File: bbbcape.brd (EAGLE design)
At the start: 54.6 x 71.8 mm, 11 parts

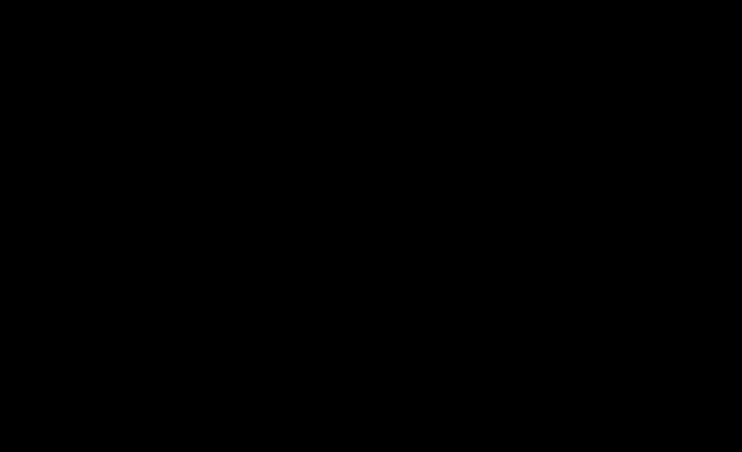
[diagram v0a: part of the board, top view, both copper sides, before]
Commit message: Connected motors.
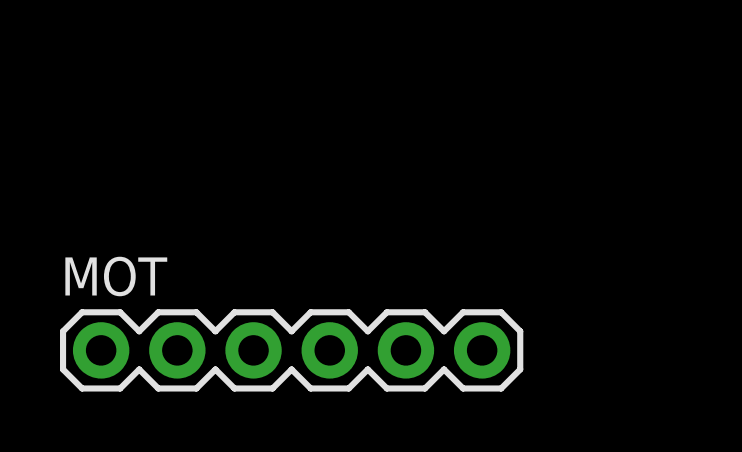
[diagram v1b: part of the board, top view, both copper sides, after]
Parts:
- added MOT: (no value), SparkFun-Connectors:1X06
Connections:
- net BC renamed BCOM
- removed net B0: BPR.2
- removed net B1: BPR.3
- removed net B2: BPR.4
- removed net B3: BPR.5
- new net BAR_DR: BBB.9, BPR.4
- new net BAR_GA: BBB.10, BPR.5
- new net BAV_DR: BBB.7, BPR.2
- new net BAV_GA: BBB.8, BPR.3
- new net DIR_MOT_DR0: BBB.58, MOT.1
- new net DIR_MOT_DR1: BBB.59, MOT.2
- new net DIR_MOT_GA0: BBB.61, MOT.4
- new net DIR_MOT_GA1: BBB.67, MOT.5
- new net PWM_MOT_DR: BBB.60, MOT.3
- new net PWM_MOT_GA: BBB.62, MOT.6
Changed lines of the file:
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@@
 <attribute name="PROD_ID" value="CONN-08437" x="-33.02" y="90.17" size="1.778" layer="27" display="off"/>
+</element>
+<element name="MOT" library="SparkFun-Connectors" package="1X06" value="" x="-82.55" y="-29.21">
+<attribute name="PROD_ID" value="CONN-08437" x="-82.55" y="-29.21" size="1.778" layer="27" display="off"/>
 </element>
 </elements>
@@
 <contactref element="SHLD1" pad="7"/>
 </signal>
-<signal name="BC">
+<signal name="BCOM">
 <contactref element="BPR" pad="1"/>
 <contactref element="R1" pad="P$1"/>
 <wire x1="-66.04" y1="95.25" x2="-41.91" y2="95.25" width="0" layer="19" extent="1-1"/>
 </signal>
-<signal name="B0">
+<signal name="BAV_DR">
 <contactref element="BPR" pad="2"/>
+<contactref element="BBB" pad="7"/>
+<wire x1="3.81" y1="8.89" x2="-39.37" y2="95.25" width="0" layer="19" extent="1-1"/>
 </signal>
-<signal name="B1">
+<signal name="BAV_GA">
 <contactref element="BPR" pad="3"/>
+<contactref element="BBB" pad="8"/>
+<wire x1="1.27" y1="8.89" x2="-36.83" y2="95.25" width="0" layer="19" extent="1-1"/>
 </signal>
-<signal name="B2">
+<signal name="BAR_DR">
 <contactref element="BPR" pad="4"/>
+<contactref element="BBB" pad="9"/>
+<wire x1="3.81" y1="11.43" x2="-34.29" y2="95.25" width="0" layer="19" extent="1-1"/>
 </signal>
-<signal name="B3">
+<signal name="BAR_GA">
 <contactref element="BPR" pad="5"/>
+<contactref element="BBB" pad="10"/>
+<wire x1="1.27" y1="11.43" x2="-31.75" y2="95.25" width="0" layer="19" extent="1-1"/>
 </signal>
 <signal name="3.3V">
@@
 <wire x1="49.53" y1="3.81" x2="52.07" y2="3.81" width="0" layer="19" extent="1-1"/>
 </signal>
+<signal name="DIR_MOT_DR0">
+<contactref element="BBB" pad="58"/>
+<contactref element="MOT" pad="1"/>
+<wire x1="49.53" y1="13.97" x2="-82.55" y2="-29.21" width="0" layer="19" extent="1-1"/>
+</signal>
+<signal name="PWM_MOT_DR">
+<contactref element="BBB" pad="60"/>
+<contactref element="MOT" pad="3"/>
+<wire x1="49.53" y1="16.51" x2="-77.47" y2="-29.21" width="0" layer="19" extent="1-1"/>
+</signal>
+<signal name="PWM_MOT_GA">
+<contactref element="BBB" pad="62"/>
+<contactref element="MOT" pad="6"/>
+<wire x1="49.53" y1="19.05" x2="-69.85" y2="-29.21" width="0" layer="19" extent="1-1"/>
+</signal>
+<signal name="DIR_MOT_DR1">
+<contactref element="BBB" pad="59"/>
+<contactref element="MOT" pad="2"/>
+<wire x1="52.07" y1="16.51" x2="-80.01" y2="-29.21" width="0" layer="19" extent="1-1"/>
+</signal>
+<signal name="DIR_MOT_GA0">
+<contactref element="BBB" pad="61"/>
+<contactref element="MOT" pad="4"/>
+<wire x1="52.07" y1="19.05" x2="-74.93" y2="-29.21" width="0" layer="19" extent="1-1"/>
+</signal>
+<signal name="DIR_MOT_GA1">
+<contactref element="BBB" pad="67"/>
+<contactref element="MOT" pad="5"/>
+<wire x1="52.07" y1="26.67" x2="-72.39" y2="-29.21" width="0" layer="19" extent="1-1"/>
+</signal>
 </signals>

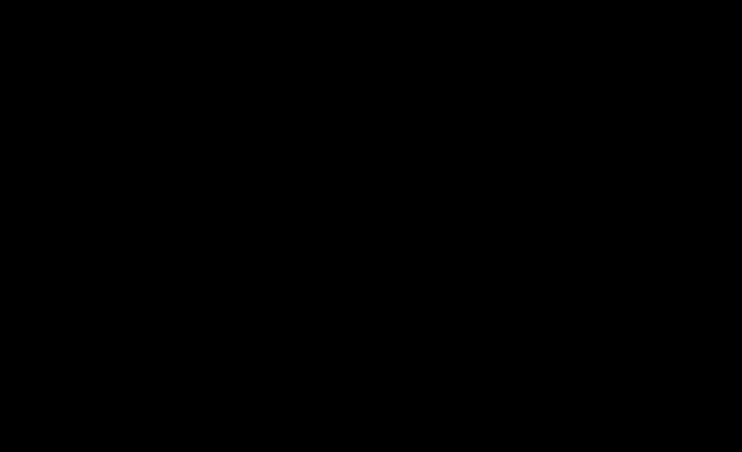
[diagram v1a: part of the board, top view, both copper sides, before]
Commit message: Connected CMUCam2+.
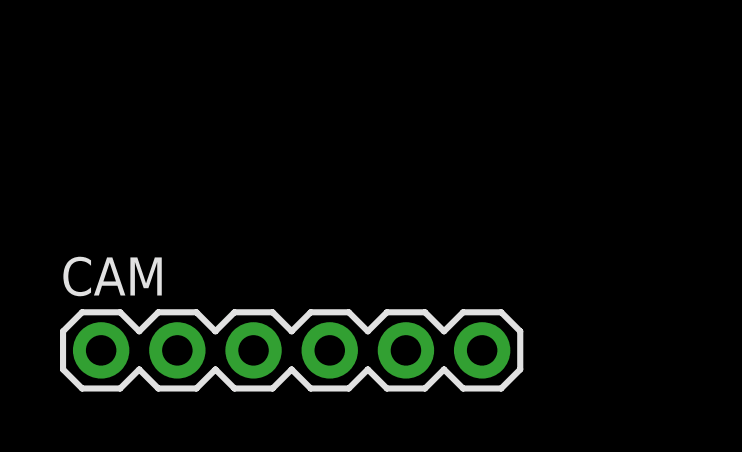
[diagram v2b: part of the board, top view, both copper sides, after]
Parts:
- added CAM: (no value), SparkFun-Connectors:1X06
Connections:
- new net UART1_RX: BBB.72, CAM.6
- new net UART1_TX: BBB.70, CAM.5
- new net VCC: CAM.2
- net 3.3V: now also CAM.3
- net 5V: now also CAM.4
- net GND: now also CAM.1
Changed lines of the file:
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@@
 <attribute name="PROD_ID" value="CONN-08437" x="-82.55" y="-29.21" size="1.778" layer="27" display="off"/>
+</element>
+<element name="CAM" library="SparkFun-Connectors" package="1X06" value="" x="-82.55" y="-48.26">
+<attribute name="PROD_ID" value="CONN-08437" x="-82.55" y="-48.26" size="1.778" layer="27" display="off"/>
 </element>
 </elements>
@@
 <contactref element="5VO" pad="5"/>
 <contactref element="5VO" pad="6"/>
+<contactref element="CAM" pad="1"/>
+<wire x1="-74.93" y1="3.81" x2="-82.55" y2="-48.26" width="0" layer="19" extent="1-1"/>
+<wire x1="1.27" y1="1.27" x2="-74.93" y2="3.81" width="0" layer="19" extent="1-1"/>
+<wire x1="3.81" y1="1.27" x2="1.27" y2="1.27" width="0" layer="19" extent="1-1"/>
+<wire x1="49.53" y1="1.27" x2="3.81" y2="1.27" width="0" layer="19" extent="1-1"/>
+<wire x1="52.07" y1="1.27" x2="49.53" y2="1.27" width="0" layer="19" extent="1-1"/>
+<wire x1="52.07" y1="54.61" x2="52.07" y2="1.27" width="0" layer="19" extent="1-1"/>
+<wire x1="52.07" y1="57.15" x2="52.07" y2="54.61" width="0" layer="19" extent="1-1"/>
+<wire x1="49.53" y1="57.15" x2="52.07" y2="57.15" width="0" layer="19" extent="1-1"/>
+<wire x1="49.53" y1="54.61" x2="52.07" y2="54.61" width="0" layer="19" extent="1-1"/>
+<wire x1="-15.24" y1="95.25" x2="49.53" y2="57.15" width="0" layer="19" extent="1-1"/>
 <wire x1="-17.78" y1="95.25" x2="-15.24" y2="95.25" width="0" layer="19" extent="1-1"/>
 <wire x1="-20.32" y1="95.25" x2="-17.78" y2="95.25" width="0" layer="19" extent="1-1"/>
@@
 <wire x1="-74.93" y1="90.17" x2="-72.39" y2="90.17" width="0" layer="19" extent="1-1"/>
 <wire x1="-77.47" y1="90.17" x2="-74.93" y2="90.17" width="0" layer="19" extent="1-1"/>
-<wire x1="52.07" y1="57.15" x2="-15.24" y2="95.25" width="0" layer="19" extent="1-1"/>
-<wire x1="52.07" y1="54.61" x2="52.07" y2="57.15" width="0" layer="19" extent="1-1"/>
-<wire x1="49.53" y1="57.15" x2="52.07" y2="57.15" width="0" layer="19" extent="1-1"/>
-<wire x1="49.53" y1="54.61" x2="52.07" y2="54.61" width="0" layer="19" extent="1-1"/>
-<wire x1="52.07" y1="1.27" x2="52.07" y2="54.61" width="0" layer="19" extent="1-1"/>
-<wire x1="49.53" y1="1.27" x2="52.07" y2="1.27" width="0" layer="19" extent="1-1"/>
-<wire x1="3.81" y1="1.27" x2="49.53" y2="1.27" width="0" layer="19" extent="1-1"/>
-<wire x1="1.27" y1="1.27" x2="3.81" y2="1.27" width="0" layer="19" extent="1-1"/>
-<wire x1="-74.93" y1="3.81" x2="1.27" y2="1.27" width="0" layer="19" extent="1-1"/>
 </signal>
 <signal name="N$1">
@@
 <contactref element="BBB" pad="52"/>
 <contactref element="BBB" pad="54"/>
+<contactref element="CAM" pad="4"/>
+<wire x1="49.53" y1="6.35" x2="-74.93" y2="-48.26" width="0" layer="19" extent="1-1"/>
+<wire x1="52.07" y1="6.35" x2="49.53" y2="6.35" width="0" layer="19" extent="1-1"/>
+<wire x1="52.07" y1="8.89" x2="52.07" y2="6.35" width="0" layer="19" extent="1-1"/>
+<wire x1="49.53" y1="8.89" x2="49.53" y2="6.35" width="0" layer="19" extent="1-1"/>
+<wire x1="-45.72" y1="95.25" x2="49.53" y2="8.89" width="0" layer="19" extent="1-1"/>
 <wire x1="-58.42" y1="95.25" x2="-45.72" y2="95.25" width="0" layer="19" extent="1-1"/>
 <wire x1="-63.5" y1="90.17" x2="-58.42" y2="95.25" width="0" layer="19" extent="1-1"/>
 <wire x1="-66.04" y1="90.17" x2="-63.5" y2="90.17" width="0" layer="19" extent="1-1"/>
-<wire x1="49.53" y1="8.89" x2="-45.72" y2="95.25" width="0" layer="19" extent="1-1"/>
-<wire x1="52.07" y1="8.89" x2="49.53" y2="8.89" width="0" layer="19" extent="1-1"/>
-<wire x1="52.07" y1="6.35" x2="52.07" y2="8.89" width="0" layer="19" extent="1-1"/>
-<wire x1="49.53" y1="6.35" x2="49.53" y2="8.89" width="0" layer="19" extent="1-1"/>
 </signal>
 <signal name="DEAD">
@@
 <contactref element="BBB" pad="49"/>
 <contactref element="BBB" pad="50"/>
-<wire x1="49.53" y1="3.81" x2="52.07" y2="3.81" width="0" layer="19" extent="1-1"/>
+<contactref element="CAM" pad="3"/>
+<wire x1="49.53" y1="3.81" x2="-77.47" y2="-48.26" width="0" layer="19" extent="1-1"/>
+<wire x1="52.07" y1="3.81" x2="49.53" y2="3.81" width="0" layer="19" extent="1-1"/>
 </signal>
 <signal name="DIR_MOT_DR0">
@@
 <wire x1="52.07" y1="26.67" x2="-72.39" y2="-29.21" width="0" layer="19" extent="1-1"/>
 </signal>
+<signal name="VCC">
+<contactref element="CAM" pad="2"/>
+</signal>
+<signal name="UART1_TX">
+<contactref element="BBB" pad="70"/>
+<contactref element="CAM" pad="5"/>
+<wire x1="49.53" y1="29.21" x2="-72.39" y2="-48.26" width="0" layer="19" extent="1-1"/>
+</signal>
+<signal name="UART1_RX">
+<contactref element="BBB" pad="72"/>
+<contactref element="CAM" pad="6"/>
+<wire x1="49.53" y1="31.75" x2="-69.85" y2="-48.26" width="0" layer="19" extent="1-1"/>
+</signal>
 </signals>

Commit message: Connected bumpers.
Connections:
- net BCOM: now also BBB.12
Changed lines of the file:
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@@
 <contactref element="BPR" pad="1"/>
 <contactref element="R1" pad="P$1"/>
+<contactref element="BBB" pad="12"/>
 <wire x1="-66.04" y1="95.25" x2="-41.91" y2="95.25" width="0" layer="19" extent="1-1"/>
+<wire x1="1.27" y1="13.97" x2="-41.91" y2="95.25" width="0" layer="19" extent="1-1"/>
 </signal>
 <signal name="BAV_DR">

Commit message: Connected GP2D12 rangefinders.
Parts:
- added R2, R4, R6, R8: 670, SparkFun-Passives:AXIAL-0.3
- added R3, R5, R7, R9: 1k, SparkFun-Passives:AXIAL-0.3
- added RF_AR_MI, RF_AV_DR, RF_AV_GA, RF_AV_MI: (no value), SparkFun-Connectors:1X03
- R1: value (none) -> 10k
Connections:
- new net AIN1: BBB.86, R4.P$1, R5.P$2
- new net AIN2: BBB.83, R2.P$1, R3.P$2
- new net AIN3: BBB.84, R8.P$1, R9.P$2
- new net N$2: R2.P$2, RF_AV_DR.3
- new net N$4: R4.P$2
- new net N$5: R6.P$2
- new net N$6: R8.P$2
- net 5V: now also RF_AV_DR.2
- net AIN0: now also R6.P$1, R7.P$2
- net GND: now also R3.P$1, R5.P$1, R7.P$1, R9.P$1, RF_AV_DR.1
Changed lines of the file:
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@@
 <attribute name="PROD_ID" value="CAP-08439" x="-73.66" y="3.81" size="1.778" layer="27" display="off"/>
 </element>
-<element name="R1" library="SparkFun-Passives" package="AXIAL-0.3" value="" x="-62.23" y="95.25"/>
+<element name="R1" library="SparkFun-Passives" package="AXIAL-0.3" value="10k" x="-62.23" y="95.25"/>
 <element name="SHLD0" library="SparkFun-Connectors" package="1X02" value="" x="-48.26" y="95.25"/>
 <element name="SHLD1" library="SparkFun-Connectors" package="1X08_ROUND" value="" x="-33.02" y="90.17">
@@
 <attribute name="PROD_ID" value="CONN-08437" x="-82.55" y="-48.26" size="1.778" layer="27" display="off"/>
 </element>
+<element name="RF_AV_DR" library="SparkFun-Connectors" package="1X03" value="" x="-82.55" y="-67.31"/>
+<element name="RF_AV_GA" library="SparkFun-Connectors" package="1X03" value="" x="-82.55" y="-86.36"/>
+<element name="RF_AV_MI" library="SparkFun-Connectors" package="1X03" value="" x="-82.55" y="-105.41"/>
+<element name="RF_AR_MI" library="SparkFun-Connectors" package="1X03" value="" x="-82.55" y="-124.46"/>
+<element name="R2" library="SparkFun-Passives" package="AXIAL-0.3" value="670" x="-78.74" y="-143.51"/>
+<element name="R3" library="SparkFun-Passives" package="AXIAL-0.3" value="1k" x="-78.74" y="-162.56"/>
+<element name="R4" library="SparkFun-Passives" package="AXIAL-0.3" value="670" x="-78.74" y="-181.61"/>
+<element name="R5" library="SparkFun-Passives" package="AXIAL-0.3" value="1k" x="-78.74" y="-200.66"/>
+<element name="R6" library="SparkFun-Passives" package="AXIAL-0.3" value="670" x="-78.74" y="-219.71"/>
+<element name="R7" library="SparkFun-Passives" package="AXIAL-0.3" value="1k" x="-78.74" y="-238.76"/>
+<element name="R8" library="SparkFun-Passives" package="AXIAL-0.3" value="670" x="-78.74" y="-257.81"/>
+<element name="R9" library="SparkFun-Passives" package="AXIAL-0.3" value="1k" x="-78.74" y="-276.86"/>
 </elements>
 <signals>
 <signal name="AIN0">
+<contactref element="R7" pad="P$2"/>
+<contactref element="R6" pad="P$1"/>
 <contactref element="BBB" pad="85"/>
+<wire x1="-82.55" y1="-219.71" x2="52.07" y2="49.53" width="0" layer="19" extent="1-1"/>
+<wire x1="-74.93" y1="-238.76" x2="-82.55" y2="-219.71" width="0" layer="19" extent="1-1"/>
 </signal>
 <signal name="GND">
@@
 <contactref element="5VO" pad="6"/>
 <contactref element="CAM" pad="1"/>
+<contactref element="R3" pad="P$1"/>
+<contactref element="RF_AV_DR" pad="1"/>
+<contactref element="R5" pad="P$1"/>
+<contactref element="R7" pad="P$1"/>
+<contactref element="R9" pad="P$1"/>
+<wire x1="-82.55" y1="-200.66" x2="-82.55" y2="-162.56" width="0" layer="19" extent="1-1"/>
+<wire x1="-82.55" y1="-238.76" x2="-82.55" y2="-200.66" width="0" layer="19" extent="1-1"/>
+<wire x1="-82.55" y1="-276.86" x2="-82.55" y2="-238.76" width="0" layer="19" extent="1-1"/>
+<wire x1="-82.55" y1="-67.31" x2="-82.55" y2="-162.56" width="0" layer="19" extent="1-1"/>
+<wire x1="-82.55" y1="-48.26" x2="-82.55" y2="-67.31" width="0" layer="19" extent="1-1"/>
 <wire x1="-74.93" y1="3.81" x2="-82.55" y2="-48.26" width="0" layer="19" extent="1-1"/>
 <wire x1="1.27" y1="1.27" x2="-74.93" y2="3.81" width="0" layer="19" extent="1-1"/>
@@
 <contactref element="BBB" pad="54"/>
 <contactref element="CAM" pad="4"/>
+<contactref element="RF_AV_DR" pad="2"/>
+<wire x1="-74.93" y1="-48.26" x2="-80.01" y2="-67.31" width="0" layer="19" extent="1-1"/>
 <wire x1="49.53" y1="6.35" x2="-74.93" y2="-48.26" width="0" layer="19" extent="1-1"/>
 <wire x1="52.07" y1="6.35" x2="49.53" y2="6.35" width="0" layer="19" extent="1-1"/>
@@
 <wire x1="49.53" y1="31.75" x2="-69.85" y2="-48.26" width="0" layer="19" extent="1-1"/>
 </signal>
+<signal name="N$2">
+<contactref element="R2" pad="P$2"/>
+<contactref element="RF_AV_DR" pad="3"/>
+<wire x1="-77.47" y1="-67.31" x2="-74.93" y2="-143.51" width="0" layer="19" extent="1-1"/>
+</signal>
+<signal name="N$4">
+<contactref element="R4" pad="P$2"/>
+</signal>
+<signal name="N$5">
+<contactref element="R6" pad="P$2"/>
+</signal>
+<signal name="N$6">
+<contactref element="R8" pad="P$2"/>
+</signal>
+<signal name="AIN2">
+<contactref element="R3" pad="P$2"/>
+<contactref element="R2" pad="P$1"/>
+<contactref element="BBB" pad="83"/>
+<wire x1="-82.55" y1="-143.51" x2="-74.93" y2="-162.56" width="0" layer="19" extent="1-1"/>
+<wire x1="52.07" y1="46.99" x2="-82.55" y2="-143.51" width="0" layer="19" extent="1-1"/>
+</signal>
+<signal name="AIN1">
+<contactref element="R5" pad="P$2"/>
+<contactref element="R4" pad="P$1"/>
+<contactref element="BBB" pad="86"/>
+<wire x1="-82.55" y1="-181.61" x2="49.53" y2="49.53" width="0" layer="19" extent="1-1"/>
+<wire x1="-74.93" y1="-200.66" x2="-82.55" y2="-181.61" width="0" layer="19" extent="1-1"/>
+</signal>
+<signal name="AIN3">
+<contactref element="BBB" pad="84"/>
+<contactref element="R9" pad="P$2"/>
+<contactref element="R8" pad="P$1"/>
+<wire x1="-82.55" y1="-257.81" x2="-74.93" y2="-276.86" width="0" layer="19" extent="1-1"/>
+<wire x1="49.53" y1="46.99" x2="-82.55" y2="-257.81" width="0" layer="19" extent="1-1"/>
+</signal>
 </signals>

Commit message: Connected shields.
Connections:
- new net VDD: 5VO.1, 5VO.2, BBB.51, BBB.52
- net 5V: no longer 5VO.1, 5VO.2, BBB.51, BBB.52
- net DEAD: now also BBB.15
- net FREE: now also BBB.29
- net GND: now also SHLD1.8
- net RESET: now also BBB.27
- net SHLD0: now also BBB.17
- net SHLD1: now also BBB.21
- net SHLD2: now also BBB.23
- net SHLD3: now also BBB.25
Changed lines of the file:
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@@
 <contactref element="R7" pad="P$1"/>
 <contactref element="R9" pad="P$1"/>
+<contactref element="SHLD1" pad="8"/>
 <wire x1="-82.55" y1="-200.66" x2="-82.55" y2="-162.56" width="0" layer="19" extent="1-1"/>
 <wire x1="-82.55" y1="-238.76" x2="-82.55" y2="-200.66" width="0" layer="19" extent="1-1"/>
@@
 <wire x1="49.53" y1="57.15" x2="52.07" y2="57.15" width="0" layer="19" extent="1-1"/>
 <wire x1="49.53" y1="54.61" x2="52.07" y2="54.61" width="0" layer="19" extent="1-1"/>
-<wire x1="-15.24" y1="95.25" x2="49.53" y2="57.15" width="0" layer="19" extent="1-1"/>
+<wire x1="-15.24" y1="90.17" x2="49.53" y2="57.15" width="0" layer="19" extent="1-1"/>
+<wire x1="-15.24" y1="95.25" x2="-15.24" y2="90.17" width="0" layer="19" extent="1-1"/>
 <wire x1="-17.78" y1="95.25" x2="-15.24" y2="95.25" width="0" layer="19" extent="1-1"/>
 <wire x1="-20.32" y1="95.25" x2="-17.78" y2="95.25" width="0" layer="19" extent="1-1"/>
@@
 </signal>
 <signal name="5V">
-<contactref element="5VO" pad="1"/>
-<contactref element="5VO" pad="2"/>
 <contactref element="SHLD0" pad="2"/>
 <contactref element="R1" pad="P$2"/>
-<contactref element="BBB" pad="51"/>
 <contactref element="BBB" pad="53"/>
-<contactref element="BBB" pad="52"/>
 <contactref element="BBB" pad="54"/>
 <contactref element="CAM" pad="4"/>
 <contactref element="RF_AV_DR" pad="2"/>
 <wire x1="-74.93" y1="-48.26" x2="-80.01" y2="-67.31" width="0" layer="19" extent="1-1"/>
-<wire x1="49.53" y1="6.35" x2="-74.93" y2="-48.26" width="0" layer="19" extent="1-1"/>
-<wire x1="52.07" y1="6.35" x2="49.53" y2="6.35" width="0" layer="19" extent="1-1"/>
-<wire x1="52.07" y1="8.89" x2="52.07" y2="6.35" width="0" layer="19" extent="1-1"/>
-<wire x1="49.53" y1="8.89" x2="49.53" y2="6.35" width="0" layer="19" extent="1-1"/>
+<wire x1="49.53" y1="8.89" x2="-74.93" y2="-48.26" width="0" layer="19" extent="1-1"/>
+<wire x1="52.07" y1="8.89" x2="49.53" y2="8.89" width="0" layer="19" extent="1-1"/>
 <wire x1="-45.72" y1="95.25" x2="49.53" y2="8.89" width="0" layer="19" extent="1-1"/>
 <wire x1="-58.42" y1="95.25" x2="-45.72" y2="95.25" width="0" layer="19" extent="1-1"/>
-<wire x1="-63.5" y1="90.17" x2="-58.42" y2="95.25" width="0" layer="19" extent="1-1"/>
-<wire x1="-66.04" y1="90.17" x2="-63.5" y2="90.17" width="0" layer="19" extent="1-1"/>
 </signal>
 <signal name="DEAD">
 <contactref element="SHLD1" pad="1"/>
+<contactref element="BBB" pad="15"/>
+<wire x1="3.81" y1="19.05" x2="-33.02" y2="90.17" width="0" layer="19" extent="1-1"/>
 </signal>
 <signal name="SHLD0">
 <contactref element="SHLD1" pad="2"/>
+<contactref element="BBB" pad="17"/>
+<wire x1="3.81" y1="21.59" x2="-30.48" y2="90.17" width="0" layer="19" extent="1-1"/>
 </signal>
 <signal name="SHLD1">
 <contactref element="SHLD1" pad="3"/>
+<contactref element="BBB" pad="21"/>
+<wire x1="3.81" y1="26.67" x2="-27.94" y2="90.17" width="0" layer="19" extent="1-1"/>
 </signal>
 <signal name="SHLD2">
 <contactref element="SHLD1" pad="4"/>
+<contactref element="BBB" pad="23"/>
+<wire x1="3.81" y1="29.21" x2="-25.4" y2="90.17" width="0" layer="19" extent="1-1"/>
 </signal>
 <signal name="SHLD3">
 <contactref element="SHLD1" pad="5"/>
+<contactref element="BBB" pad="25"/>
+<wire x1="3.81" y1="31.75" x2="-22.86" y2="90.17" width="0" layer="19" extent="1-1"/>
 </signal>
 <signal name="RESET">
 <contactref element="SHLD1" pad="6"/>
+<contactref element="BBB" pad="27"/>
+<wire x1="3.81" y1="34.29" x2="-20.32" y2="90.17" width="0" layer="19" extent="1-1"/>
 </signal>
 <signal name="FREE">
 <contactref element="SHLD1" pad="7"/>
+<contactref element="BBB" pad="29"/>
+<wire x1="3.81" y1="36.83" x2="-17.78" y2="90.17" width="0" layer="19" extent="1-1"/>
 </signal>
 <signal name="BCOM">
@@
 <wire x1="49.53" y1="46.99" x2="-82.55" y2="-257.81" width="0" layer="19" extent="1-1"/>
 </signal>
+<signal name="VDD">
+<contactref element="BBB" pad="51"/>
+<contactref element="5VO" pad="1"/>
+<contactref element="5VO" pad="2"/>
+<contactref element="BBB" pad="52"/>
+<wire x1="49.53" y1="6.35" x2="52.07" y2="6.35" width="0" layer="19" extent="1-1"/>
+<wire x1="-63.5" y1="90.17" x2="49.53" y2="6.35" width="0" layer="19" extent="1-1"/>
+<wire x1="-66.04" y1="90.17" x2="-63.5" y2="90.17" width="0" layer="19" extent="1-1"/>
+</signal>
 </signals>
